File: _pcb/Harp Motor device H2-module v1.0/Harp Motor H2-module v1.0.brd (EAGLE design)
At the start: 102 x 60.8 mm, 73 parts, among them IC1 FT232RL, IC2 74VHC1GT126DT1G, IC3 LP5907MFX-3.3, IC4 74VHC1GT126DT1G, IC5 74VHC1GT126DT1G, IC7 USBLC6-2SC6, IC8 ATXMEGA32A4U, IC9 TLV70033DDCR, T1 DMG1012UW??, T2 DMG1012UW??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

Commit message: Harp Motor device H2-module v1.0 - Schematic step on
Harp Motor device H2-module v1.0 - Schematic step on
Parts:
- removed C15, C16: 100nF, rcl:C0402K
- removed HARP: Harp_Intrfc, con-weidmueller-sl35:90G-5
- removed R10: 0R, rcl:R0402@1
- removed R11: DNI, rcl:R0402@1
- removed R4, R7: 10k, rcl:R0402@1
- removed R9: 1M, rcl:R0402@1
- added H2_MAIN_PLUG: be sure about plug type, Harp Motor H2-module v1.0:90G-5
- added IC6: 74AHC1G125DBV, Harp Motor H2-module v1.0:SOT23-5
- added PWR1: DC_JACK2.1MM, harp camera controller:DC_POWER_INPUT_2.1MM
- C1, C12, C13, C14, C17, C2, C25, C26, C27, C28, C29, C3, C4, C5, C6, C7, C9: device rcl:C0402K -> Harp Motor H2-module v1.0:C0402K
- C10, C11: device rcl:C0603K -> Harp Motor H2-module v1.0:C0603K
- C8: device rcl:C0603 -> Harp Motor H2-module v1.0:C0603
- D4: device diode:SOT23 -> Harp Motor H2-module v1.0:SOT23
- L1, L2: device rcl:R0603 -> Harp Motor H2-module v1.0:R0603
- R1, R12, R13, R18, R2, R3, R34, R5, R6, R8: device rcl:R0402@1 -> Harp Motor H2-module v1.0:R0402$1
- STATE: device led:CHIP-LED0603 -> Harp Motor H2-module v1.0:CHIP-LED0603
- SV2: device Connector:2X03 -> Harp Motor H2-module v1.0:2X03
- TP1, TP10, TP11, TP13: device testpad:B1,27 -> Harp Motor H2-module v1.0:B1,27
- TP4, TP5, TP6, TP8, TP9: device testpad:TP11R -> Harp Motor H2-module v1.0:TP11R
- X2, X7: device con-molex:22-23-2051 -> Harp Motor H2-module v1.0:22-23-2051
- X3: device con-molex:22-23-2021 -> Harp Motor H2-module v1.0:22-23-2021
- X4: device con-molex:22-23-2031 -> Harp Motor H2-module v1.0:22-23-2031
- X6: device SparkFun-Connectors:BNC -> Harp Motor H2-module v1.0:BNC
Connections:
- net A_PHASE renamed ENCODER_A_PHASE
- net B_PHASE renamed ENCODER_B_PHASE
- net U_A_PHASE renamed U_ENCODER_A_PHASE
- net U_B_PHASE renamed U_ENCODER_B_PHASE
- removed net +12V: D4.3, HARP.1
- removed net HARP_H1_CLOCK_IN: HARP.4
- removed net HARP_H1_RX: HARP.3
- removed net HARP_H1_TX: HARP.2
- removed net LICK_PORT_1: R9.2
- removed net N$5: C1.1, IC2.5, R10.2, R11.2, X4.3
- removed net N$6: D4.1
- new net HARP_H2_CLOCK_IN: H2_MAIN_PLUG.4, IC8.26
- new net HARP_H2_RX: H2_MAIN_PLUG.3, IC8.25
- new net HARP_H2_TX: H2_MAIN_PLUG.2, IC8.24
- new net N$4: X7.1
- new net VCC: IC6.5
- new net VDD: H2_MAIN_PLUG.1, PWR1.P1
- net +3V3: now also C1.1, IC2.5, X4.2; no longer R10.1
- net +5V: no longer R11.1, X7.1
- net GND: now also H2_MAIN_PLUG.5, IC6.3, PWR1.P2, PWR1.P3, X4.3; no longer C15.2, C16.2, HARP.5, R4.1, R7.1, R9.1, X4.1, X6.GND
- net HALL_EFFCT_IN: now also X4.1; no longer X4.2

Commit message: Harp Motor device H2-module v1.0 - design proceeding
Harp Motor device H2-module v1.0 - design proceeding
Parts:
- removed IC2, IC4, IC5: 74VHC1GT126DT1G, VestibularVR H1-module v1.0:SOT23-5
- removed IC6: 74AHC1G125DBV, Harp Motor H2-module v1.0:SOT23-5
- removed X6: BNCPTH, Harp Motor H2-module v1.0:BNC
- added IC11, IC12, IC13: 74LVC1G125DBV, Harp Motor H2-module v1.0:SOT23-5
- added R4: 0R, Harp Motor H2-module v1.0:R0402$1
- added R7: 10k, Harp Motor H2-module v1.0:R0402$1
- R13: value 10k -> DNI
- moved CLKIN 80.2 mm to (17.1, 47.3), turned to 270 degrees
- moved PWR1 57.4 mm to (53.0, 4.86)
- moved TP11 55.7 mm to (37.0, 5.84)
- moved TP10 52.2 mm to (9.67, 37.4)
- moved R1 40.7 mm to (20.2, 25.2)
- moved STATE 37.0 mm to (22.2, 25.2), turned to 0 degrees
- moved TP13 36.7 mm to (38.8, 31.6)
- moved H2_MAIN_PLUG 33.7 mm to (53.4, 22.9)
- moved C28 32.7 mm to (30.0, 2.06), turned to 180 degrees
- moved TP9 32.3 mm to (33.2, 3.80)
- moved C29 31.9 mm to (19.5, 9.62)
- moved C12 31.8 mm to (41.9, 19.7), turned to 180 degrees
- moved C26 31.7 mm to (38.1, 14.4)
- moved C25 31.6 mm to (32.2, 20.5)
- moved IC8 31.5 mm to (29.0, 11.4)
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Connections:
- removed net N$4: X7.1
- removed net V+: R8.2
- removed net VCC: IC6.5
- new net AREF: IC8.40, R4.1, R7.2
- net +3V3: now also C14.1, C17.1, IC11.5, IC12.5, IC13.5; no longer IC2.5
- net +3V3_U: now also R4.2, R8.2
- net +5V: now also X7.1; no longer C14.1, C17.1, IC4.5, IC5.5
- net ENCODER_A_PHASE: now also IC11.2; no longer IC4.2
- net ENCODER_B_PHASE: now also IC12.2; no longer IC5.2
- net GND: now also IC11.1, IC11.3, IC12.1, IC12.3, IC13.1, IC13.3, R7.1; no longer IC2.3, IC4.3, IC5.3, IC6.3
- net HALL_EFFCT_IN: now also IC13.2; no longer IC2.2
- net U_ENCODER_A_PHASE: now also IC11.4; no longer IC4.4
- net U_ENCODER_B_PHASE: now also IC12.4; no longer IC5.4
- net U_HALL_EFFCT_IN: now also IC13.4, IC8.41; no longer IC2.4, IC8.40
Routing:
- net +3V3: track 107.9 -> 48.8 mm, vias 7 -> 4
- net EMERGENCY_INPUT: track 0.00 -> 56.3 mm, vias 0 -> 1
- net CLOCK_IN: track 0.00 -> 36.5 mm, vias 0 -> 2
- net LED_STATE: track 34.9 -> 0.00 mm, vias 3 -> 0
- net U_ENCODER_A_PHASE: track 0.00 -> 30.7 mm, vias 0 -> 2
- net U_HALL_EFFCT_IN: track 0.00 -> 28.6 mm, vias 0 -> 2
- net HARP_H2_CLOCK_IN: track 0.00 -> 28.6 mm, vias 0 -> 1
- net HARP_H2_RX: track 0.00 -> 26.2 mm, vias 0 -> 1
- net U_ENCODER_B_PHASE: track 0.00 -> 25.8 mm, vias 0 -> 2
- net HARP_H2_TX: track 0.00 -> 23.9 mm, vias 0 -> 1
- net U_STEP_PULSE: track 0.00 -> 20.6 mm, vias 0 -> 2
- net U_STEP_DIRECTION: track 0.00 -> 18.7 mm, vias 0 -> 2
- net U_STEP_ENABLE: track 0.00 -> 17.5 mm
- net +3V3_U: track 107.1 -> 123.4 mm, vias 9 -> 5
- net VDD: track 0.00 -> 15.7 mm
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- added copper zone on layer 1, net GND
- added copper zone on layer 16, net GND
- removed copper zone on layer 1, net +3V3
- removed copper zone on layer 15, net +3V3
- removed copper zone on layer 16, net +3V3
- removed copper zone on layer 2, net +3V3
- removed copper zone on layer 1, net +5V
- removed copper zone on layer 15, net +5V
- removed copper zone on layer 16, net +5V
- removed copper zone on layer 2, net +5V
- removed copper zone on layer 1, net N$10
- removed copper zone on layer 15, net N$100
- removed copper zone on layer 1, net N$101
- removed copper zone on layer 1, net N$106
- removed copper zone on layer 1, net N$107
- removed copper zone on layer 1, net N$108
- removed copper zone on layer 15, net N$110
- removed copper zone on layer 1, net N$16
- removed copper zone on layer 1, net N$24
- removed copper zone on layer 1, net N$25
- removed copper zone on layer 1, net N$26
- removed copper zone on layer 1, net N$27
- removed copper zone on layer 1, net N$45
- removed copper zone on layer 1, net N$46
- removed copper zone on layer 1, net N$48
- removed copper zone on layer 1, net N$54
- removed copper zone on layer 1, net N$55
- removed copper zone on layer 1, net N$56
- removed copper zone on layer 2, net N$58
- removed copper zone on layer 1, net N$59
- removed copper zone on layer 1, net N$60
- removed copper zone on layer 15, net N$61
- removed copper zone on layer 16, net N$62
- removed copper zone on layer 1, net N$7
- removed copper zone on layer 1, net N$75
- removed copper zone on layer 1, net N$76
- removed copper zone on layer 1, net N$77
- removed copper zone on layer 15, net N$78
- removed copper zone on layer 15, net N$99
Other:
- board size 102 x 60.8 mm -> 62 x 56.6 mm
- board text added: "Emergency Butt input"
- board text added: "Hall effect sensor input"
- board text added: "Rotary Encoder input"
- board text added: "Step Motor control output"

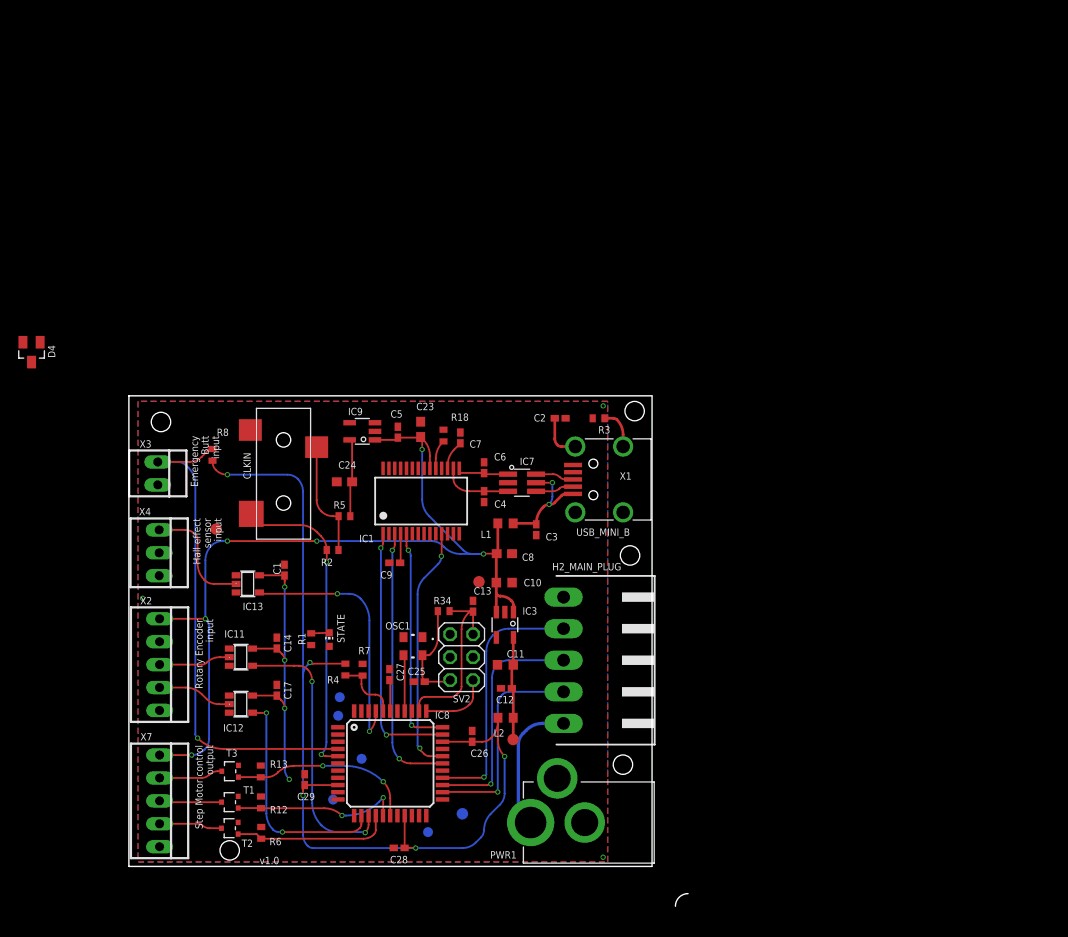
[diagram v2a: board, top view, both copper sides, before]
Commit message: Harp Motor device H2-module v1.0 - 1st 'finished' version
Harp Motor device H2-module v1.0 - 1st 'finished' version
- missing:
   . some schm & pcb review with Filipe
   . components order codes & BOM
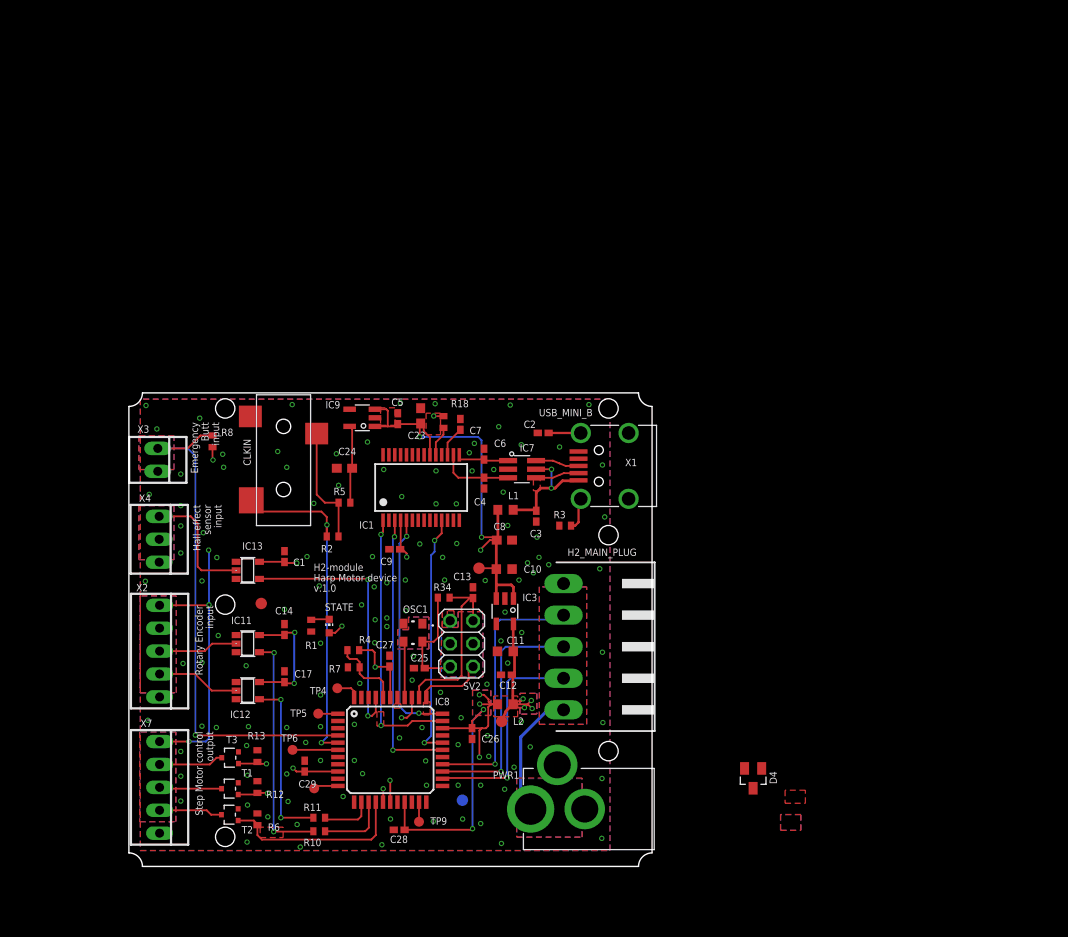
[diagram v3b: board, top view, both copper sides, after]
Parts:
- added R10, R11: 0R, Harp Motor H2-module v1.0:R0402$1
- moved D4 92.9 mm to (69.2, 9.77)
- moved R3 12.5 mm to (48.4, 37.8)
- moved TP10 9.65 mm to (14.7, 29.2)
- moved TP6 7.72 mm to (18.1, 12.9), flipped to the top
- moved C2 2.48 mm to (45.9, 48.1), turned to 180 degrees
- moved TP8 2.44 mm to (20.5, 8.66), flipped to the top
- moved TP1 2.38 mm to (41.3, 16.1)
- moved R4 2.32 mm to (24.9, 24.0), turned to 0 degrees
- moved TP5 2.23 mm to (21.0, 16.9), flipped to the top
- moved C28 2.00 mm to (30.0, 4.06)
- moved R12 1.75 mm to (14.2, 8.80)
- moved R13 1.74 mm to (14.2, 12.2)
- moved C14 1.72 mm to (17.2, 26.3)
- moved C17 1.72 mm to (17.2, 21.0)
- moved IC11 1.68 mm to (13.2, 24.7)
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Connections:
- new net N$59: IC8.14, R10.1
- new net N$60: IC8.13, R11.1
- net N$1: now also X1.SHIELD_4; no longer X1.SHIELD_2
- net U_ENCODER_A_PHASE: now also R10.2; no longer IC8.14
- net U_ENCODER_B_PHASE: now also R11.2; no longer IC8.13
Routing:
- net +3V3: track 48.8 -> 221.2 mm, vias 4 -> 14
- net +3V3_U: track 123.4 -> 170.9 mm, vias 5 -> 9
- net LED_STATE: track 0.00 -> 20.6 mm, vias 0 -> 3
- net +5V: track 103.8 -> 113.1 mm
- net N$59: track 0.00 -> 7.85 mm
- net U_ENCODER_B_PHASE: track 25.8 -> 19.1 mm
- net N$60: track 0.00 -> 5.81 mm
- net N$13: track 0.00 -> 5.03 mm
- net U_ENCODER_A_PHASE: track 30.7 -> 25.9 mm
- net U_STEP_ENABLE: track 17.5 -> 20.7 mm
- net N$17: track 0.00 -> 2.74 mm
- net N$11: track 0.00 -> 2.70 mm
- net CLOCK_IN: track 36.5 -> 39.1 mm
- net N$12: track 0.00 -> 2.19 mm
- net N$18: track 0.00 -> 2.17 mm
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- added copper zone on layer 1, net +3V3
- added copper zone on layer 15, net +3V3
- added copper zone on layer 16, net +3V3
- added copper zone on layer 2, net +3V3
- added copper zone on layer 1, net +3V3_U
- added copper zone on layer 15, net +3V3_U
- added copper zone on layer 16, net +3V3_U
- added copper zone on layer 2, net +3V3_U
- added copper zone on layer 15, net GND
- added copper zone on layer 2, net GND
- added copper zone on layer 15, net N$10
- added copper zone on layer 2, net N$14
- added copper zone on layer 1, net N$16
- added copper zone on layer 16, net N$19
- added copper zone on layer 15, net N$20
- added copper zone on layer 2, net N$21
- added copper zone on layer 1, net N$22
- added copper zone on layer 16, net N$23
- added copper zone on layer 15, net N$24
- added copper zone on layer 2, net N$25
- added copper zone on layer 1, net N$26
- added copper zone on layer 16, net N$27
- added copper zone on layer 15, net N$28
- added copper zone on layer 2, net N$29
- added copper zone on layer 1, net N$30
- added copper zone on layer 16, net N$31
- added copper zone on layer 15, net N$32
- added copper zone on layer 2, net N$33
- added copper zone on layer 1, net N$34
- added copper zone on layer 16, net N$35
- added copper zone on layer 15, net N$36
- added copper zone on layer 2, net N$37
- added copper zone on layer 1, net N$39
- added copper zone on layer 16, net N$4
- added copper zone on layer 15, net N$40
- added copper zone on layer 2, net N$41
- added copper zone on layer 1, net N$42
- added copper zone on layer 15, net N$43
- added copper zone on layer 16, net N$44
- added copper zone on layer 2, net N$45
- added copper zone on layer 2, net N$46
- added copper zone on layer 1, net N$47
- added copper zone on layer 15, net N$48
- added copper zone on layer 16, net N$49
- added copper zone on layer 15, net N$5
- added copper zone on layer 1, net N$50
- added copper zone on layer 1, net N$51
- added copper zone on layer 1, net N$52
- added copper zone on layer 1, net N$53
- added copper zone on layer 1, net N$54
- added copper zone on layer 1, net N$55
- added copper zone on layer 1, net N$56
- added copper zone on layer 1, net N$57
- added copper zone on layer 1, net N$58
- added copper zone on layer 2, net N$6
- added copper zone on layer 1, net N$61
- added copper zone on layer 1, net N$7
- added copper zone on layer 16, net N$8
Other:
- board size 62 x 56.6 mm -> 58 x 52.5 mm
- board text added: "H2-module Harp Motor device v.1.0"
- board text removed: "v1.0"

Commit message: Harp Motor device H2-module v1.0; commit after revision
Harp Motor device H2-module v1.0:
- commit after revisions made with Filipe @Dezember 14th 2022
- missing components OEPS code & BOM
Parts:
- removed D4: BAT54, Harp Motor H2-module v1.0:SOT23
- removed IC13: 74LVC1G125DBV, Harp Motor H2-module v1.0:SOT23-5
- removed R10, R11: 0R, Harp Motor H2-module v1.0:R0402$1
- added C15: 4.7uF DNI, Harp Motor H2-module v1.0:C0603K
- added C16: 100nF, Harp Motor H2-module v1.0:C0402K
- added C41, C42: 15nF 5%, rcl:C0402
- added IC10: OPA365, CNP-ics 2:SOT23-5
- added L3: 40R@100MHz, Harp Motor H2-module v1.0:R0805
- added R14, R15, R16: DNI, Harp Motor H2-module v1.0:R0402$1
- added R17, R19: 10k 1%, rcl:R0402
- added R20: 24k, rcl:R0402
- added R21: 15k, rcl:R0402
- added R9: 100R DNI, Harp Motor H2-module v1.0:R0402$1
- L1, L2: device Harp Motor H2-module v1.0:R0603 -> Harp Motor H2-module v1.0:R0805
- R4: value 0R -> 0R DNI
- R7: value 10k -> 10k DNI
- moved R8 2.90 mm to (9.37, 44.2), flipped to the bottom, turned to 180 degrees
- moved C1 1.98 mm to (17.8, 32.4), flipped to the bottom, turned to 270 degrees
- moved R7 1.91 mm to (23.0, 22.3), flipped to the bottom, turned to 270 degrees
- moved R4 1.70 mm to (24.9, 22.3), flipped to the bottom, turned to 90 degrees
- moved R6 0.90 mm to (14.2, 6.12)
- moved T1 0.73 mm to (11.0, 9.32)
- moved T3 0.73 mm to (11.0, 12.8)
- moved T2 0.73 mm to (11.0, 6.44)
- moved R12 0.60 mm to (14.2, 9.40)
- moved R13 0.60 mm to (14.2, 12.8)
- moved TP1 0.50 mm to (41.8, 16.1)
- moved L2 0.30 mm to (41.4, 18.0)
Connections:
- removed net N$59: IC8.14, R10.1
- removed net N$60: IC8.13, R11.1
- new net N$50: C41.2, R17.2, R19.1
- new net N$62: C15.1, R4.2, R9.1
- new net N$63: C16.1, IC8.39, L3.1
- new net N$64: IC10.1, IC10.4, R17.1
- new net N$65: IC10.3, R20.1, R21.2
- net +3V3: now also IC10.5; no longer IC13.5
- net +3V3_U: now also L3.2, R9.2; no longer IC8.39, R4.2
- net +5V: now also R14.2, R15.2, R16.2
- net CLOCK_IN: now also IC8.12; no longer IC8.5
- net GND: now also C15.2, C16.2, C41.1, C42.1, IC10.2, IC8.42, R21.1; no longer IC13.1, IC13.3
- net HALL_EFFCT_IN: now also R20.2; no longer IC13.2
- net STEP_DIRECTION: now also R15.1
- net STEP_ENABLE: now also R16.1
- net STEP_PULSE: now also R14.1
- net U_ENCODER_A_PHASE: now also IC8.15; no longer R10.2
- net U_ENCODER_B_PHASE: now also IC8.14; no longer R11.2
- net U_HALL_EFFCT_IN: now also C42.2, R19.2; no longer IC13.4
- net U_STEP_ENABLE: now also IC8.13; no longer IC8.15
- net U_STEP_PULSE: now also IC8.10; no longer IC8.17
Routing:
- net U_ENCODER_A_PHASE: track 25.9 -> 36.9 mm
- net U_ENCODER_B_PHASE: track 19.1 -> 27.7 mm
- net +5V: track 113.1 -> 121.3 mm
- net CLOCK_IN: track 39.1 -> 47.2 mm
- net N$59: track 7.85 -> 0.00 mm
- net HALL_EFFCT_IN: track 13.8 -> 6.23 mm
- net U_STEP_PULSE: track 20.7 -> 13.2 mm
- net N$64: track 0.00 -> 7.08 mm
- net N$63: track 0.00 -> 6.38 mm, vias 0 -> 1
- net U_HALL_EFFCT_IN: track 29.8 -> 23.8 mm
- net N$60: track 5.81 -> 0.00 mm
- net N$65: track 0.00 -> 5.52 mm
- net U_STEP_ENABLE: track 20.7 -> 15.4 mm
- net N$62: track 0.00 -> 4.99 mm
- net STEP_PULSE: track 7.21 -> 12.2 mm
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- added copper zone on layer 16, net N$40
- added copper zone on layer 1, net N$45
- added copper zone on layer 1, net N$46
- added copper zone on layer 1, net N$48
- added copper zone on layer 1, net N$49
- removed copper zone on layer 15, net N$40
- removed copper zone on layer 2, net N$45
- removed copper zone on layer 2, net N$46
- removed copper zone on layer 15, net N$48
- removed copper zone on layer 16, net N$49
- removed copper zone on layer 1, net N$50
- removed copper zone on layer 1, net N$51
